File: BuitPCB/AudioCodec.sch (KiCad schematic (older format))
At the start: 7 parts, among them J4 AudioJack3, J6 AudioJack3, U3 AP7361C-33E, U4 SGTL5000XNAA3

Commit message: Updated adding battery management sheet and componnents to PCB
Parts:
- U3: footprint Package_TO_SOT_SMD:SOT-223-3_TabPin2 -> Package_TO_SOT_SMD:SOT-23
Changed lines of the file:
@@
 $Descr A4 11693 8268
 encoding utf-8
-Sheet 4 6
+Sheet 3 7
 Title ""
 Date ""
@@
 F 0 "U3" H 2650 2492 50  0000 C CNN
 F 1 "AP7361C-33E" H 2650 2401 50  0000 C CNN
-F 2 "Package_TO_SOT_SMD:SOT-223-3_TabPin2" H 2650 2475 50  0001 C CIN
+F 2 "Package_TO_SOT_SMD:SOT-23" H 2650 2475 50  0001 C CIN
 F 3 "https://www.diodes.com/assets/Datasheets/AP7361C.pdf" H 2650 2200 50  0001 C CNN
 	1    2650 2250

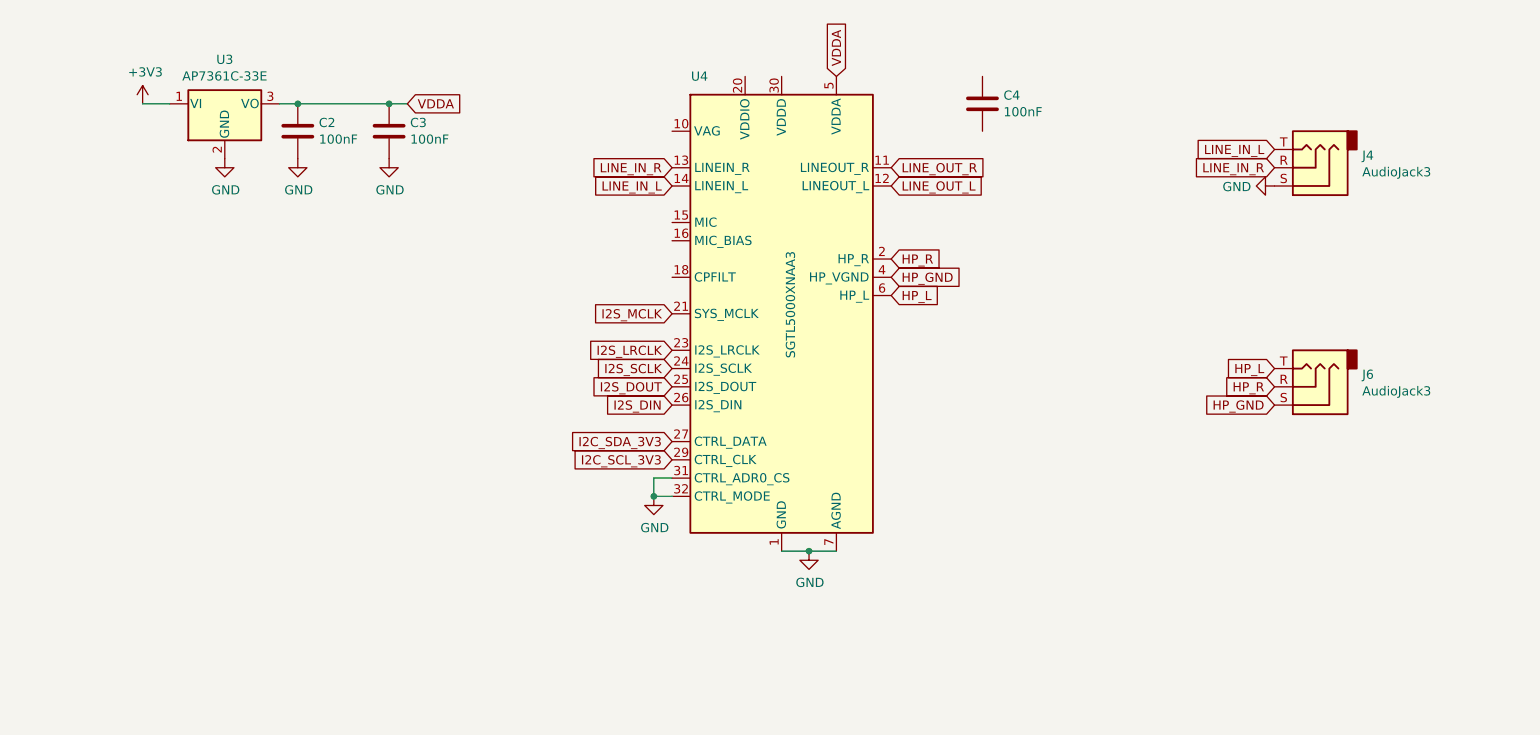
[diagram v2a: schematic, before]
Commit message: Updated to almost every component and started routing
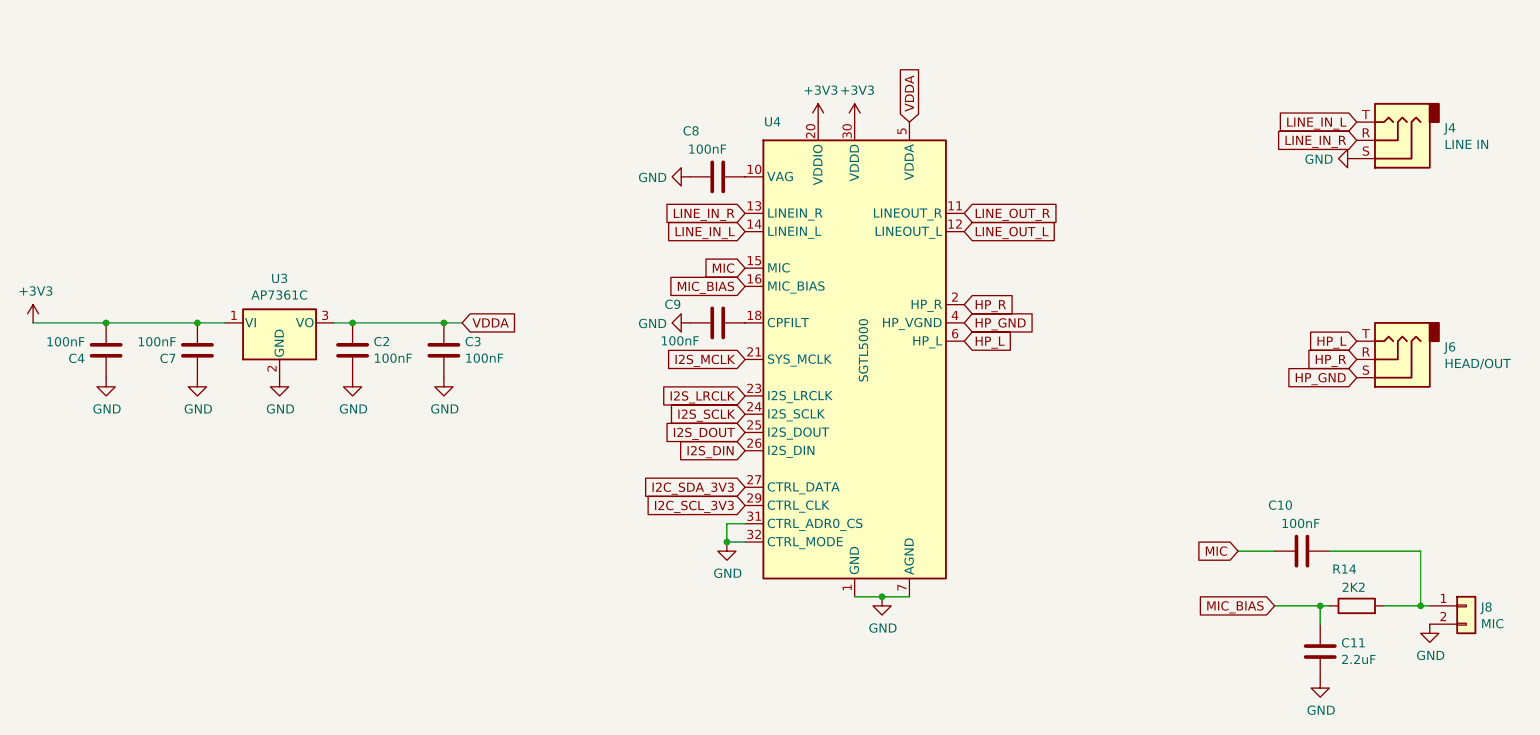
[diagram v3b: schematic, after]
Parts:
- added C10, C7, C8, C9: 100nF, Capacitor_SMD:C_0805_2012Metric, symbol Device:C
- added C11: 2.2uF, Capacitor_SMD:C_0805_2012Metric, symbol Device:C
- added J8: MIC, Connector_JST:JST_XH_B2B-XH-A_1x02_P2.50mm_Vertical, symbol Connector_Generic:Conn_01x02
- added R14: 2K2, Resistor_SMD:R_0805_2012Metric, symbol Device:R
- J4: value AudioJack3 -> LINE IN
- J6: value AudioJack3 -> HEAD/OUT
- U3: value AP7361C-33E -> AP7361C
- U4: value SGTL5000XNAA3 -> SGTL5000
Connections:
- net +3V3: now also C4.2, U4.20 (VDDIO), U4.30 (VDDD), C7.2
- net GND: now also C4.1, C11.2, C7.1, C8.1, C9.1, J8.2 (Pin_2)
- net at U4.10 (VAG): now also C8.2
- net MIC: now reaches U4.15 (MIC)
- net MIC: now also C10.1
- net MIC_BIAS: now reaches U4.16 (MIC_BIAS)
- net MIC_BIAS: now also C11.1, R14.1
- net at U4.18 (CPFILT): now also C9.2
- new net: C10.2, J8.1 (Pin_1), R14.2
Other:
- moved on the sheet: C2, C3, J4, J6, U3, U4
